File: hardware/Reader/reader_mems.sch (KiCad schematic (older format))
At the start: 2 parts

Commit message: Fixed numerous bugs in design for Reader Schematic and PCB
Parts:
- C_MM_1: footprint footprints:FA16C0G2A104JRU06 -> footprints:CAPC1608X90N
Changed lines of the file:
@@
 $Descr USLetter 11000 8500
 encoding utf-8
-Sheet 19 19
+Sheet 14 19
 Title "CANnect Reader | MEMs"
 Date "2020-11-19"
@@
 Comment4 "Component Identifier: MM"
 $EndDescr
+Text HLabel 3100 3900 0    50   Input ~ 0
+MEMS_INT2
+Text HLabel 3100 3400 0    50   BiDi ~ 0
+MEMS_SDO_SA0
+Text HLabel 3100 3100 0    50   Input ~ 0
+MEMS_CS
+Text HLabel 3100 3800 0    50   Input ~ 0
+MEMS_INT1
+Text HLabel 3100 3300 0    50   BiDi ~ 0
+MEMS_SDA
+Text HLabel 3100 3200 0    50   BiDi ~ 0
+MEMS_SCL
 $Comp
 L power:+3.3V #PWR089
@@
 F 0 "C_MM_1" H 7865 3196 50  0000 L CNN
 F 1 "100nF" H 7865 3105 50  0000 L CNN
-F 2 "footprints:FA16C0G2A104JRU06" H 7788 3000 50  0001 C CNN
-F 3 "https://product.tdk.com/info/en/catalog/datasheets/leadmlcc_halogenfree_fa_en.pdf" H 7750 3150 50  0001 C CNN
+F 2 "footprints:CAPC1608X90N" H 7788 3000 50  0001 C CNN
+F 3 "https://product.tdk.com/info/en/catalog/datasheets/mlcc_commercial_midvoltage_en.pdf" H 7750 3150 50  0001 C CNN
 F 4 "C1608X7R2A103K080AA" H 7750 3150 50  0001 C CNN "Part Name"
 F 5 "DigiKey Canada" H 7750 3150 50  0001 C CNN "Vendor"
@@
 	1    0    0    -1
 $EndComp
-Text HLabel 3100 3900 0    50   Input ~ 0
-MEMS_INT2
-Text HLabel 3100 3400 0    50   BiDi ~ 0
-MEMS_SDO_SA0
-Text HLabel 3100 3100 0    50   Input ~ 0
-MEMS_CS
-Text HLabel 3100 3800 0    50   Input ~ 0
-MEMS_INT1
-Text HLabel 3100 3300 0    50   BiDi ~ 0
-MEMS_SDA
-Text HLabel 3100 3200 0    50   BiDi ~ 0
-MEMS_SCL
 Wire Wire Line
 	3100 3900 5650 3900

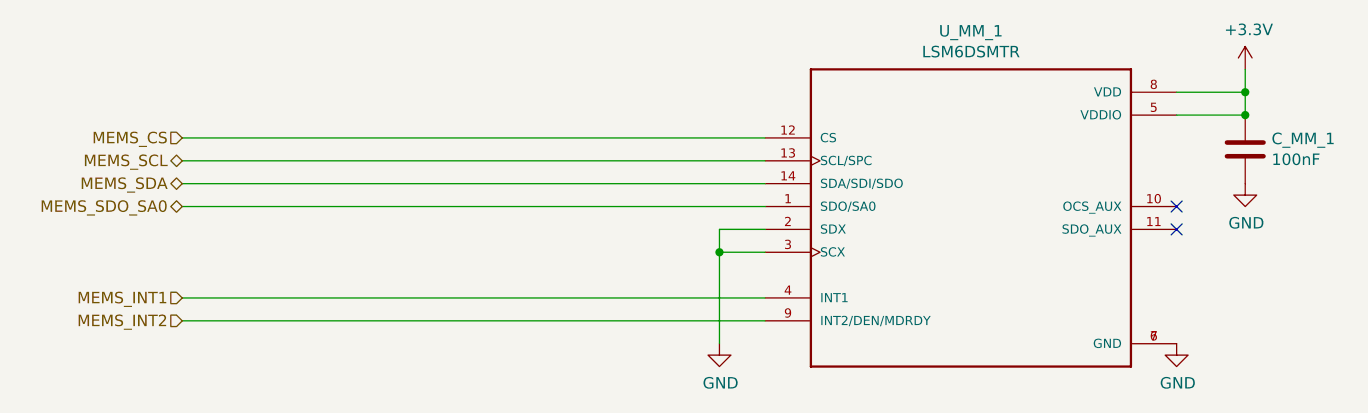
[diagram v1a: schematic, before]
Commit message: Updated reader schematic to v0.0.5 by adding ESP32, removing unused transceivers, fixed design flaws, increased header pins and fixed footprints. Working on reader PCB design
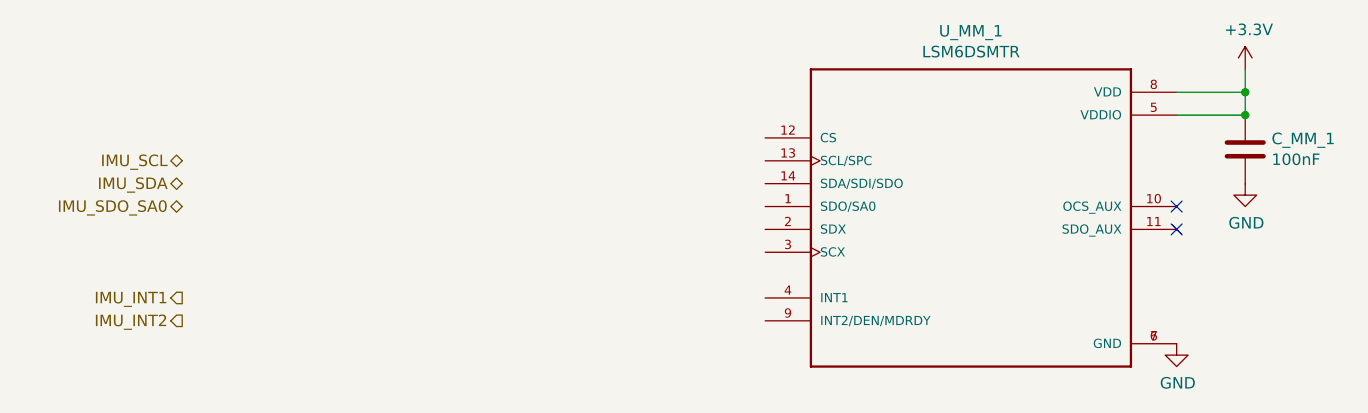
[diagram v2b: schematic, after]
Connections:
- net GND: no longer U_MM_1.2 (SDX), U_MM_1.3 (SCX)
- net MEMS_CS: no longer names the net of U_MM_1.12 (CS)
- net MEMS_INT1: no longer names the net of U_MM_1.4 (INT1)
- net MEMS_INT2: no longer names the net of U_MM_1.9 (INT2/DEN/MDRDY)
- net MEMS_SCL: no longer names the net of U_MM_1.13 (SCL/SPC)
- net MEMS_SDA: no longer names the net of U_MM_1.14 (SDA/SDI/SDO)
- net MEMS_SDO_SA0: no longer names the net of U_MM_1.1 (SDO/SA0)
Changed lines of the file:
@@
 Comment4 "Component Identifier: MM"
 $EndDescr
-Text HLabel 3100 3900 0    50   Input ~ 0
-MEMS_INT2
-Text HLabel 3100 3400 0    50   BiDi ~ 0
-MEMS_SDO_SA0
-Text HLabel 3100 3100 0    50   Input ~ 0
-MEMS_CS
-Text HLabel 3100 3800 0    50   Input ~ 0
-MEMS_INT1
-Text HLabel 3100 3300 0    50   BiDi ~ 0
-MEMS_SDA
-Text HLabel 3100 3200 0    50   BiDi ~ 0
-MEMS_SCL
-$Comp
-L power:+3.3V #PWR089
-U 1 1 5FC85156
-P 7750 2800
-F 0 "#PWR089" H 7750 2650 50  0001 C CNN
-F 1 "+3.3V" H 7765 2973 50  0000 C CNN
-F 2 "" H 7750 2800 50  0001 C CNN
-F 3 "" H 7750 2800 50  0001 C CNN
-	1    7750 2800
-	1    0    0    -1
-$EndComp
-NoConn ~ 7450 3500
-NoConn ~ 7450 3400
-Wire Wire Line
-	7450 3000 7750 3000
-Wire Wire Line
-	7750 2900 7750 2800
-Wire Wire Line
-	7750 2900 7750 3000
-Connection ~ 7750 2900
-Wire Wire Line
-	7450 2900 7750 2900
-$Comp
-L power:GND #PWR?
-U 1 1 5F9A4430
-P 7750 3300
-AR Path="/5F9A4430" Ref="#PWR?"  Part="1"
-AR Path="/5F988046/5F9A4430" Ref="#PWR090"  Part="1"
-F 0 "#PWR090" H 7750 3050 50  0001 C CNN
-F 1 "GND" H 7755 3127 50  0000 C CNN
-F 2 "" H 7750 3300 50  0001 C CNN
-F 3 "" H 7750 3300 50  0001 C CNN
-	1    7750 3300
-	1    0    0    -1
-$EndComp
-Wire Wire Line
-	5450 3600 5450 3500
-Wire Wire Line
-	5650 3600 5450 3600
-Wire Wire Line
-	5450 3500 5650 3500
-Connection ~ 5450 3600
-Wire Wire Line
-	5450 4000 5450 3600
-$Comp
-L power:GND #PWR?
-U 1 1 5F9A4425
-P 5450 4000
-AR Path="/5F9A4425" Ref="#PWR?"  Part="1"
-AR Path="/5F988046/5F9A4425" Ref="#PWR087"  Part="1"
-F 0 "#PWR087" H 5450 3750 50  0001 C CNN
-F 1 "GND" H 5455 3827 50  0000 C CNN
-F 2 "" H 5450 4000 50  0001 C CNN
-F 3 "" H 5450 4000 50  0001 C CNN
-	1    5450 4000
-	1    0    0    -1
-$EndComp
-Connection ~ 7750 3000
-$Comp
-L Device:C C_MM_?
-U 1 1 5F9A441F
-P 7750 3150
-AR Path="/5F9A441F" Ref="C_MM_?"  Part="1"
-AR Path="/5F988046/5F9A441F" Ref="C_MM_1"  Part="1"
-F 0 "C_MM_1" H 7865 3196 50  0000 L CNN
-F 1 "100nF" H 7865 3105 50  0000 L CNN
-F 2 "footprints:CAPC1608X90N" H 7788 3000 50  0001 C CNN
-F 3 "https://product.tdk.com/info/en/catalog/datasheets/mlcc_commercial_midvoltage_en.pdf" H 7750 3150 50  0001 C CNN
-F 4 "C1608X7R2A103K080AA" H 7750 3150 50  0001 C CNN "Part Name"
-F 5 "DigiKey Canada" H 7750 3150 50  0001 C CNN "Vendor"
-F 6 "TDK Corporation" H 7750 3150 50  0001 C CNN "Manufacturer"
-F 7 "445-1304-1-ND" H 7750 3150 50  0001 C CNN "digikeypn"
-	1    7750 3150
-	1    0    0    -1
-$EndComp
-$Comp
-L power:GND #PWR?
-U 1 1 5F9A4413
-P 7450 4000
-AR Path="/5F9A4413" Ref="#PWR?"  Part="1"
-AR Path="/5F988046/5F9A4413" Ref="#PWR088"  Part="1"
-F 0 "#PWR088" H 7450 3750 50  0001 C CNN
-F 1 "GND" H 7455 3827 50  0000 C CNN
-F 2 "" H 7450 4000 50  0001 C CNN
-F 3 "" H 7450 4000 50  0001 C CNN
-	1    7450 4000
-	1    0    0    -1
-$EndComp
 $Comp
 L LSM6DSMTR:LSM6DSMTR U_MM_?
@@
 	1    0    0    -1
 $EndComp
+$Comp
+L power:GND #PWR?
+U 1 1 5F9A4413
+P 7450 4000
+AR Path="/5F9A4413" Ref="#PWR?"  Part="1"
+AR Path="/5F988046/5F9A4413" Ref="#PWR088"  Part="1"
+F 0 "#PWR088" H 7450 3750 50  0001 C CNN
+F 1 "GND" H 7455 3827 50  0000 C CNN
+F 2 "" H 7450 4000 50  0001 C CNN
+F 3 "" H 7450 4000 50  0001 C CNN
+	1    7450 4000
+	1    0    0    -1
+$EndComp
+$Comp
+L Device:C C_MM_?
+U 1 1 5F9A441F
+P 7750 3150
+AR Path="/5F9A441F" Ref="C_MM_?"  Part="1"
+AR Path="/5F988046/5F9A441F" Ref="C_MM_1"  Part="1"
+F 0 "C_MM_1" H 7865 3196 50  0000 L CNN
+F 1 "100nF" H 7865 3105 50  0000 L CNN
+F 2 "footprints:CAPC1608X90N" H 7788 3000 50  0001 C CNN
+F 3 "https://product.tdk.com/info/en/catalog/datasheets/mlcc_commercial_midvoltage_en.pdf" H 7750 3150 50  0001 C CNN
+F 4 "C1608X7R2A103K080AA" H 7750 3150 50  0001 C CNN "Part Name"
+F 5 "DigiKey Canada" H 7750 3150 50  0001 C CNN "Vendor"
+F 6 "TDK Corporation" H 7750 3150 50  0001 C CNN "Manufacturer"
+F 7 "445-1304-1-ND" H 7750 3150 50  0001 C CNN "digikeypn"
+	1    7750 3150
+	1    0    0    -1
+$EndComp
+$Comp
+L power:GND #PWR?
+U 1 1 5F9A4430
+P 7750 3300
+AR Path="/5F9A4430" Ref="#PWR?"  Part="1"
+AR Path="/5F988046/5F9A4430" Ref="#PWR090"  Part="1"
+F 0 "#PWR090" H 7750 3050 50  0001 C CNN
+F 1 "GND" H 7755 3127 50  0000 C CNN
+F 2 "" H 7750 3300 50  0001 C CNN
+F 3 "" H 7750 3300 50  0001 C CNN
+	1    7750 3300
+	1    0    0    -1
+$EndComp
 Wire Wire Line
-	3100 3900 5650 3900
+	7450 2900 7750 2900
 Wire Wire Line
-	5650 3100 3100 3100
+	7750 2900 7750 3000
+Connection ~ 7750 2900
 Wire Wire Line
-	5650 3400 3100 3400
+	7750 2900 7750 2800
+Connection ~ 7750 3000
 Wire Wire Line
-	3100 3200 5650 3200
-Wire Wire Line
-	5650 3300 3100 3300
-Wire Wire Line
-	3100 3800 5650 3800
+	7450 3000 7750 3000
+NoConn ~ 7450 3400
+NoConn ~ 7450 3500
+$Comp
+L power:+3.3V #PWR089
+U 1 1 5FC85156
+P 7750 2800
+F 0 "#PWR089" H 7750 2650 50  0001 C CNN
+F 1 "+3.3V" H 7765 2973 50  0000 C CNN
+F 2 "" H 7750 2800 50  0001 C CNN
+F 3 "" H 7750 2800 50  0001 C CNN
+	1    7750 2800
+	1    0    0    -1
+$EndComp
+Text HLabel 3100 3200 0    50   BiDi ~ 0
+IMU_SCL
+Text HLabel 3100 3300 0    50   BiDi ~ 0
+IMU_SDA
+Text HLabel 3100 3800 0    50   Output ~ 0
+IMU_INT1
+Text HLabel 3100 3400 0    50   BiDi ~ 0
+IMU_SDO_SA0
+Text HLabel 3100 3900 0    50   Output ~ 0
+IMU_INT2
 $EndSCHEMATC
